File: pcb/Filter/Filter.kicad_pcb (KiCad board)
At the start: 2 copper layers, 100 x 100 mm, 8 parts, among them J1 Conn_01x01, J2 Conn_01x01, J3 Conn_01x02

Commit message: filter + backplane
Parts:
- moved J3 1.92 mm to (123.1, 114.2)
- moved R1 1.00 mm to (131.0, 128.9)
- moved C1 0.51 mm to (113.6, 99.0)
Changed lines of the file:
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@@
 	(footprint "Resistor_THT:R_Axial_DIN0617_L17.0mm_D6.0mm_P25.40mm_Horizontal"
 		(layer "F.Cu")
-		(at 131 129.9 -90)
+		(at 131 128.9 -90)
 		(descr "Resistor, Axial_DIN0617 series, Axial, Horizontal, pin pitch=25.4mm, 2W, length*diameter=17*6mm^2, http://www.vishay.com/docs/20128/wkxwrx.pdf")
 		(tags "Resistor Axial_DIN0617 series Axial Horizontal pin pitch 25.4mm 2W length 17mm diameter 6mm")
@@
 	(footprint "Capacitor_THT:C_Rect_L26.5mm_W11.5mm_P22.50mm_MKS4"
 		(layer "F.Cu")
-		(at 114.1 98.85 -90)
+		(at 113.6 98.95 -90)
 		(descr "C, Rect series, Radial, pin pitch=22.50mm, , length*width=26.5*11.5mm^2, Capacitor, http://www.wima.com/EN/WIMA_MKS_4.pdf")
 		(tags "C Rect series Radial pin pitch 22.50mm  length 26.5mm width 11.5mm Capacitor")
@@
 	(footprint "Connector_Phoenix_SPT:PhoenixContact_SPT_5_2-H-7.5-ZB_1x02_P7.5mm_Horizontal"
 		(layer "F.Cu")
-		(at 124.2925 112.65 90)
+		(at 123.0925 114.15 90)
 		(descr "Connector Phoenix Contact, SPT 5/2-H-7.5-ZB Terminal Block, 1719192 (https://www.phoenixcontact.com/online/portal/gb/?uri=pxc-oc-itemdetail:pid=1719192), generated with kicad-footprint-generator")
 		(tags "Connector Phoenix Contact SPT 5/2-H-7.5-ZB 1719192")
@@
 	)
 	(segment
-		(start 131 155.3)
-		(end 117.15 155.3)
+		(start 116.15 154.3)
+		(end 106.85 145)
 		(width 2)
 		(layer "B.Cu")
@@
 	)
 	(segment
-		(start 117.15 155.3)
-		(end 106.85 145)
+		(start 131 154.3)
+		(end 116.15 154.3)
 		(width 2)
 		(layer "B.Cu")
@@
 	)
 	(zone
+		(net 0)
+		(net_name "")
+		(layers "F&B.Cu" "Edge.Cuts")
+		(hatch edge 0.5)
+		(connect_pads
+			(clearance 0)
+		)
+		(min_thickness 0.25)
+		(filled_areas_thickness no)
+		(keepout
+			(tracks not_allowed)
+			(vias allowed)
+			(pads allowed)
+			(copperpour not_allowed)
+			(footprints allowed)
+		)
+		(fill
+			(thermal_gap 0.5)
+			(thermal_bridge_width 0.5)
+		)
+		(polygon
+			(pts
+				(xy 73.1 142.8) (xy 80.4 142.8) (xy 80.4 150) (xy 73.1 150)
+			)
+		)
+	)
+	(zone
+		(net 0)
+		(net_name "")
+		(layers "F&B.Cu" "Edge.Cuts")
+		(hatch edge 0.5)
+		(connect_pads
+			(clearance 0)
+		)
+		(min_thickness 0.25)
+		(filled_areas_thickness no)
+		(keepout
+			(tracks not_allowed)
+			(vias allowed)
+			(pads allowed)
+			(copperpour not_allowed)
+			(footprints allowed)
+		)
+		(fill
+			(thermal_gap 0.5)
+			(thermal_bridge_width 0.5)
+		)
+		(polygon
+			(pts
+				(xy 73.2 70.4) (xy 80.5 70.4) (xy 80.5 77.6) (xy 73.2 77.6)
+			)
+		)
+	)
+	(zone
 		(net 2)
 		(net_name "/phb")
@@
 		(polygon
 			(pts
-				(xy 40.3 140.2) (xy 94 140.3) (xy 94 159.2) (xy 40.3 159.2)
+				(xy 40.3 140.3) (xy 93.4 140.4) (xy 93.4 159.3) (xy 40.3 159.3)
 			)
 		)
@@
 		(polygon
 			(pts
-				(xy 112.7 111.2) (xy 138.6 111.2) (xy 138.7 131.2) (xy 112.9 131.2) (xy 112.9 111.1)
+				(xy 112.3 112.7) (xy 138.6 112.7) (xy 138.6 131.4) (xy 112.3 131.4)
 			)
 		)
@@
 		(polygon
 			(pts
-				(xy 40.6 68.5) (xy 93.4 68.6) (xy 93.5 90.5) (xy 40.6 90.4)
+				(xy 40.6 68.5) (xy 93.4 68.5) (xy 93.4 90.4) (xy 40.6 90.4)
 			)
 		)
@@
 		(polygon
 			(pts
-				(xy 113.2 92.6) (xy 139 92.7) (xy 139 106.6) (xy 113.2 106.6) (xy 113.2 92.6)
-			)
-		)
+				(xy 112.3 92.6) (xy 139 92.7) (xy 139 108) (xy 112.3 108)
+			)
+		)

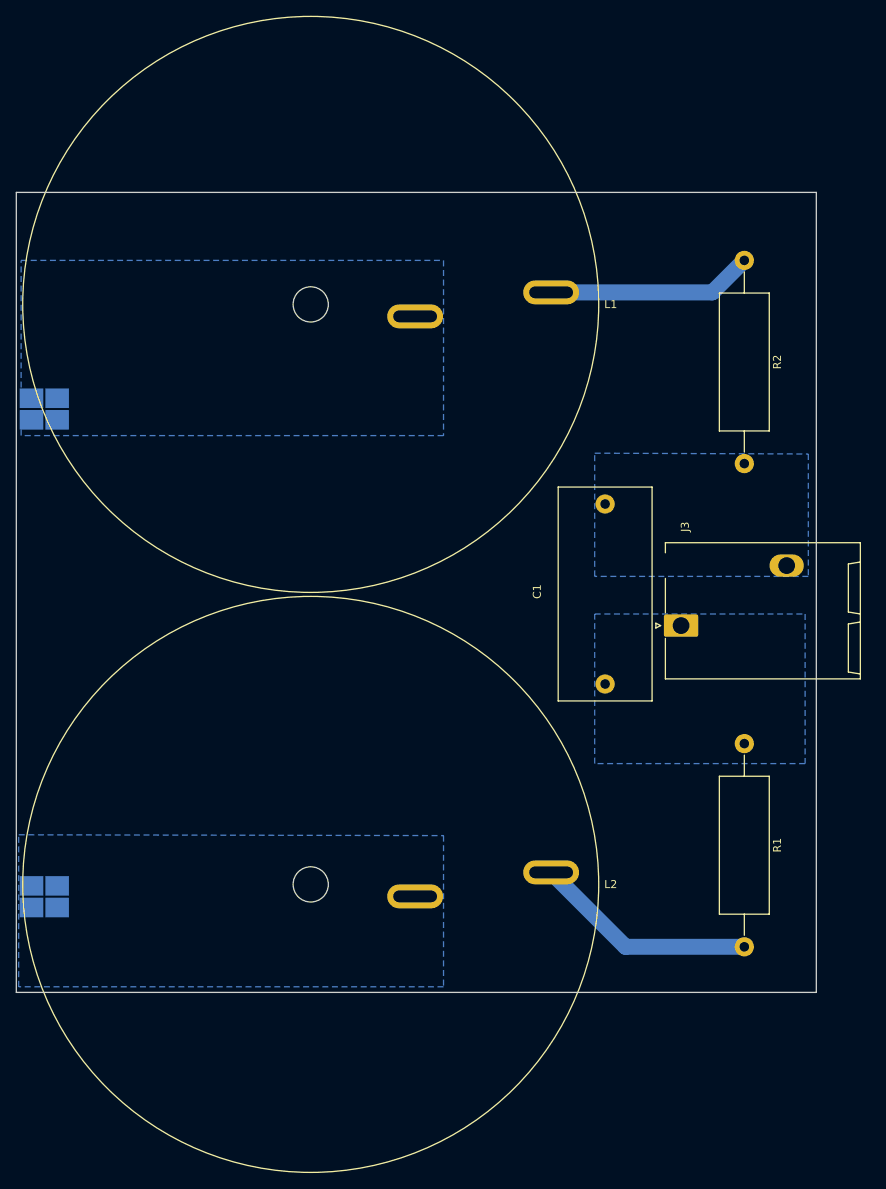
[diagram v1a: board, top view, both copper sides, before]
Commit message: new 3d filter
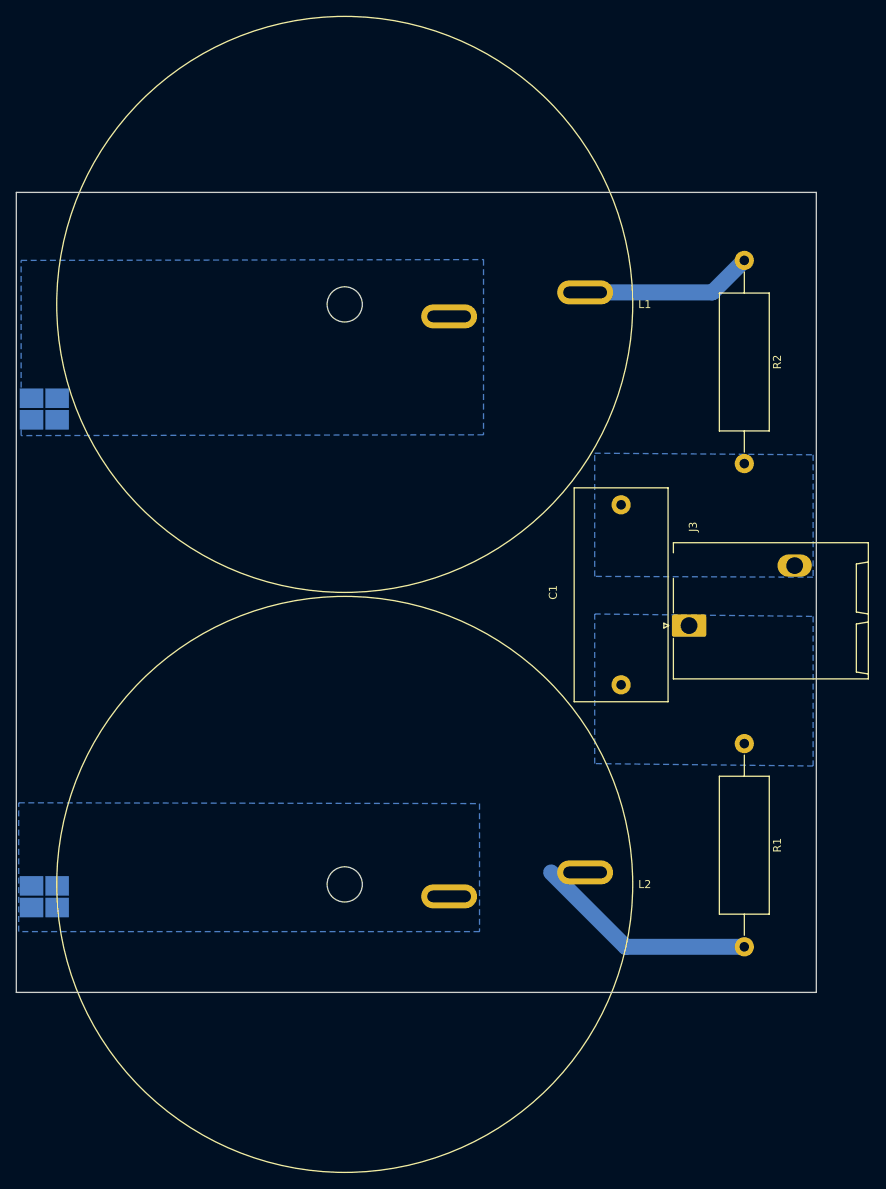
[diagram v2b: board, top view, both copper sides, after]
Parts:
- moved L1 4.25 mm to (81.0, 74.0)
- moved L2 4.25 mm to (81.0, 146.5)
- moved C1 2.00 mm to (115.6, 99.0)
- moved J3 1.00 mm to (124.1, 114.2)
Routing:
- net Net-(L1-Pad2): track 25.8 -> 21.6 mm
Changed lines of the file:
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@@
 	(footprint "My_Inductor_THT:L_Wuerth_WE-TORPFC_Diameter72.0mm_760801203"
 		(layer "F.Cu")
-		(at 76.8 74)
+		(at 81.05 74)
 		(property "Reference" "L1"
 			(at 37.5 0 0)
@@
 	(footprint "My_Inductor_THT:L_Wuerth_WE-TORPFC_Diameter72.0mm_760801203"
 		(layer "F.Cu")
-		(at 76.8 146.5)
+		(at 81.05 146.5)
 		(property "Reference" "L2"
 			(at 37.5 0 0)
@@
 	(footprint "Capacitor_THT:C_Rect_L26.5mm_W11.5mm_P22.50mm_MKS4"
 		(layer "F.Cu")
-		(at 113.6 98.95 -90)
+		(at 115.6 99.05 -90)
 		(descr "C, Rect series, Radial, pin pitch=22.50mm, , length*width=26.5*11.5mm^2, Capacitor, http://www.wima.com/EN/WIMA_MKS_4.pdf")
 		(tags "C Rect series Radial pin pitch 22.50mm  length 26.5mm width 11.5mm Capacitor")
@@
 	(footprint "Connector_Phoenix_SPT:PhoenixContact_SPT_5_2-H-7.5-ZB_1x02_P7.5mm_Horizontal"
 		(layer "F.Cu")
-		(at 123.0925 114.15 90)
+		(at 124.0925 114.15 90)
 		(descr "Connector Phoenix Contact, SPT 5/2-H-7.5-ZB Terminal Block, 1719192 (https://www.phoenixcontact.com/online/portal/gb/?uri=pxc-oc-itemdetail:pid=1719192), generated with kicad-footprint-generator")
 		(tags "Connector Phoenix Contact SPT 5/2-H-7.5-ZB 1719192")
@@
 	)
 	(segment
-		(start 106.85 72.5)
-		(end 127 72.5)
+		(start 127 72.5)
+		(end 131 68.5)
 		(width 2)
 		(layer "B.Cu")
@@
 	)
 	(segment
-		(start 127 72.5)
-		(end 131 68.5)
+		(start 111.1 72.5)
+		(end 127 72.5)
 		(width 2)
 		(layer "B.Cu")
@@
 		(polygon
 			(pts
-				(xy 73.1 142.8) (xy 80.4 142.8) (xy 80.4 150) (xy 73.1 150)
+				(xy 77.3 142.7) (xy 84.6 142.7) (xy 84.6 149.9) (xy 77.3 149.9)
 			)
 		)
@@
 		(polygon
 			(pts
-				(xy 73.2 70.4) (xy 80.5 70.4) (xy 80.5 77.6) (xy 73.2 77.6)
+				(xy 77.4 70.3) (xy 84.7 70.3) (xy 84.7 77.5) (xy 77.4 77.5)
 			)
 		)
@@
 		(polygon
 			(pts
-				(xy 40.3 140.3) (xy 93.4 140.4) (xy 93.4 159.3) (xy 40.3 159.3)
+				(xy 40.3 136.3) (xy 97.9 136.4) (xy 97.9 152.4) (xy 40.3 152.4)
 			)
 		)
@@
 		(polygon
 			(pts
-				(xy 112.3 112.7) (xy 138.6 112.7) (xy 138.6 131.4) (xy 112.3 131.4)
+				(xy 112.3 112.7) (xy 139.6 113) (xy 139.6 131.7) (xy 112.3 131.4)
 			)
 		)
@@
 		(polygon
 			(pts
-				(xy 40.6 68.5) (xy 93.4 68.5) (xy 93.4 90.4) (xy 40.6 90.4)
+				(xy 40.6 68.5) (xy 98.4 68.4) (xy 98.4 90.3) (xy 40.6 90.4)
 			)
 		)
@@
 		(polygon
 			(pts
-				(xy 112.3 92.6) (xy 139 92.7) (xy 139 108) (xy 112.3 108)
-			)
-		)
+				(xy 112.3 92.6) (xy 139.6 92.8) (xy 139.6 108.1) (xy 112.3 108)
+			)
+		)

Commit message: titles
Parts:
- added H1: MountingHole, MountingHole:MountingHole_2.7mm_M2.5, F.Cu at (43.1, 63.1)
- added H2: MountingHole, MountingHole:MountingHole_2.7mm_M2.5, F.Cu at (136.9, 63.1)
- added H3: MountingHole, MountingHole:MountingHole_2.7mm_M2.5, F.Cu at (136.9, 156.9)
- added H4: MountingHole, MountingHole:MountingHole_2.7mm_M2.5, F.Cu at (43.1, 156.9)
- moved R1 0.70 mm to (130.3, 128.9)
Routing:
- net Net-(L2-Pad2): track 28.0 -> 23.1 mm
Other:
- board text added: "${TITLE} ./pcb/${PROJECTNAME} ${COMPANY} Issued: ${ISSUE_DATE} Rev: ${REVISION} ${COMMENT1}"
- board text added: "FOa FOb"
- board text added: "H"
- board text added: "PHa"
- board text added: "PHb"
- board text added: "Rev: ${REVISION} ${COMMENT1}"
